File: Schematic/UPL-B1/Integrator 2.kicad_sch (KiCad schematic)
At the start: 61 parts, among them P40 TestPoint

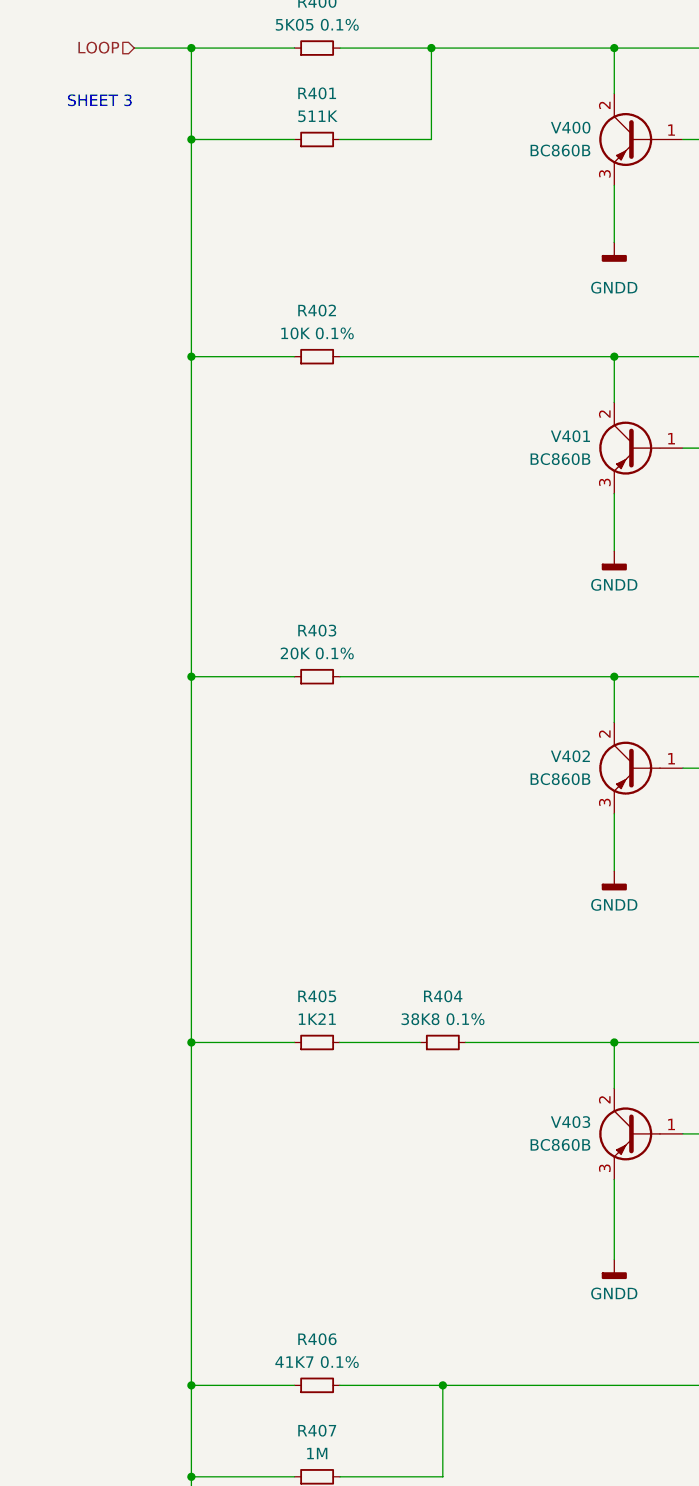
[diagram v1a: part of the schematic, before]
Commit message: Annotate with reverse engineering clues
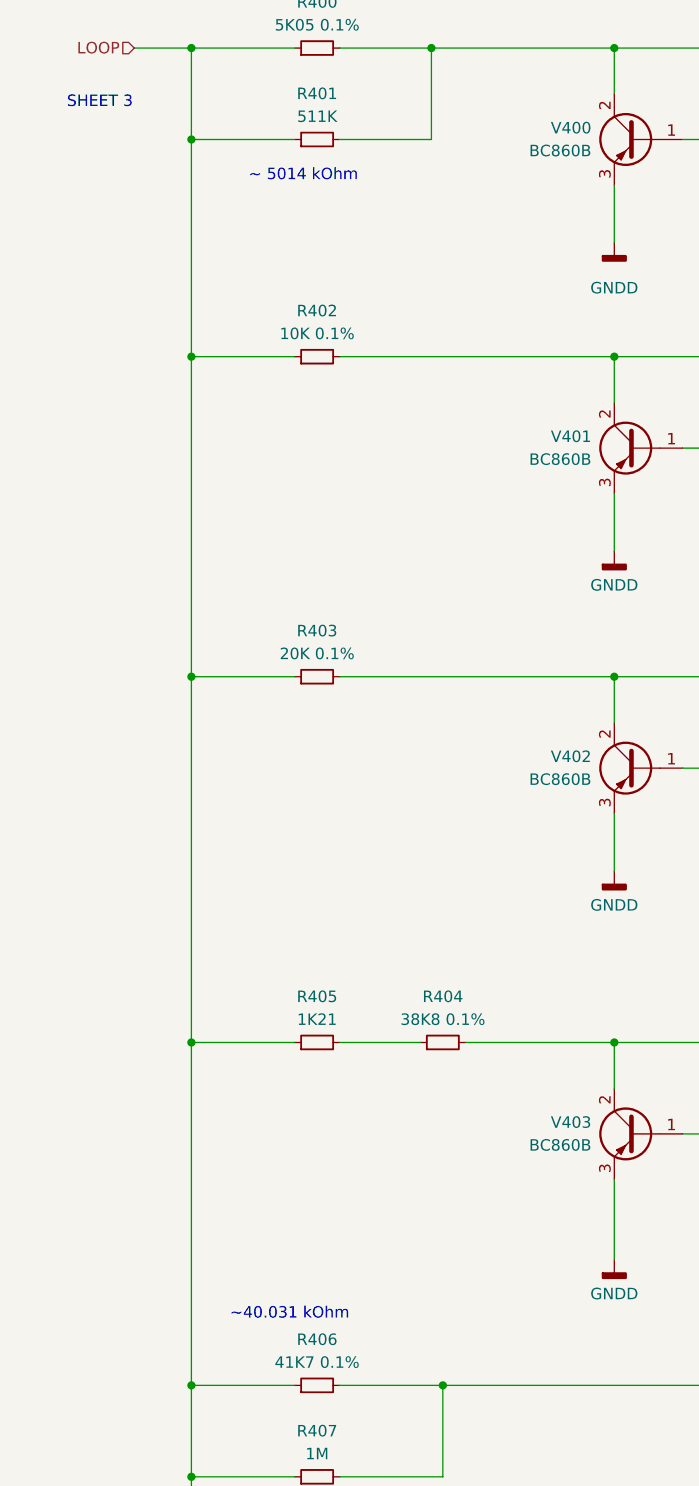
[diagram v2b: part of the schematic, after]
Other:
- note added: "~ 5014 kOhm"
- note added: "~40.031 kOhm"
